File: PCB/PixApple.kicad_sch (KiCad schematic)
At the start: 21 parts, among them J3 Conn_01x17, J4 Conn_01x17, J5 Conn_01x05_Pin, J6 Conn_01x02_Pin, SW1 SW_Push, U1 RP2040

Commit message: CAN bus done?
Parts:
- added J7: Conn_01x01_Pin, symbol Connector:Conn_01x01_Pin
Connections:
- net can/CLKOUT: now also J7.1 (Pin_1)
- net can/CANL: now reaches J6.1 (Pin_1)
- net can/CANH: now reaches J6.2 (Pin_2)
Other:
- sheet can: file can.kicad_sch -> canctrl.kicad_sch
- sheet can ports: added CANH, CANL; removed RXCAN, TXCAN
- note added: "label better"
- moved on the sheet: J6

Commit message: Routing PCB
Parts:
- removed J3, J4: Conn_01x17, symbol Connector_Generic:Conn_01x17
- added D2, D3: LED_Small, LED_SMD:LED_0603_1608Metric_Pad1.05x0.95mm_HandSolder, symbol Device:LED_Small
- added J10, J11, J12, J13, J14, J15, J16, J17, J18, J19, J20, J21, J22, J23, J24, J25, J26, J27: Conn_01x03_Pin, Connector_PinHeader_2.54mm:PinHeader_1x03_P2.54mm_Vertical, symbol Connector:Conn_01x03_Pin
- added J8: Conn_02x03_Odd_Even, Connector_PinHeader_2.54mm:PinHeader_2x03_P2.54mm_Vertical, symbol Connector_Generic:Conn_02x03_Odd_Even
- added J9: Conn_01x04_Pin, Connector_PinHeader_2.54mm:PinHeader_1x04_P2.54mm_Vertical, symbol Connector:Conn_01x04_Pin
- added R13, R14: 220R, Resistor_SMD:R_0603_1608Metric_Pad0.98x0.95mm_HandSolder, symbol Device:R_Small
- C10, C11, C12, C13, C17, C3, C4, C5, C6, C7, C8, C9: footprint (none) -> Capacitor_SMD:C_0603_1608Metric_Pad1.08x0.95mm_HandSolder
- J5: footprint (none) -> Connector_PinHeader_2.54mm:PinHeader_1x05_P2.54mm_Vertical
- J6: footprint (none) -> Connector_PinHeader_2.54mm:PinHeader_1x02_P2.54mm_Vertical
- J7: footprint (none) -> TestPoint:TestPoint_Pad_1.0x1.0mm
- R4, R5, R6: footprint (none) -> Resistor_SMD:R_0603_1608Metric_Pad0.98x0.95mm_HandSolder
- SW1: footprint (none) -> Button_Switch_THT:SW_PUSH_6mm_H5mm
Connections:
- net +3V3: now also D3.2 (A), J10.2 (Pin_2), J11.2 (Pin_2), J12.2 (Pin_2), J13.2 (Pin_2), J14.2 (Pin_2), J15.2 (Pin_2), J16.2 (Pin_2), J17.2 (Pin_2), J18.2 (Pin_2), J19.2 (Pin_2), J20.2 (Pin_2), J21.2 (Pin_2), J22.2 (Pin_2), J23.2 (Pin_2), J24.2 (Pin_2), J25.2 (Pin_2), J26.2 (Pin_2), J27.2 (Pin_2), J8.1 (Pin_1), J9.3 (Pin_3)
- net GND: now also J10.1 (Pin_1), J11.1 (Pin_1), J12.1 (Pin_1), J13.1 (Pin_1), J14.1 (Pin_1), J15.1 (Pin_1), J16.1 (Pin_1), J17.1 (Pin_1), J18.1 (Pin_1), J19.1 (Pin_1), J20.1 (Pin_1), J21.1 (Pin_1), J22.1 (Pin_1), J23.1 (Pin_1), J24.1 (Pin_1), J25.1 (Pin_1), J26.1 (Pin_1), J27.1 (Pin_1), J8.6 (Pin_6), J9.4 (Pin_4), R13.1, R14.2
- net GPIO0: now also J18.3 (Pin_3)
- net GPIO1: now also J19.3 (Pin_3)
- net GPIO12: now also J26.3 (Pin_3)
- net GPIO13: now also J27.3 (Pin_3)
- net GPIO2: now also J20.3 (Pin_3)
- net GPIO3: now also J21.3 (Pin_3)
- net GPIO4: now also J22.3 (Pin_3)
- net GPIO5: now also J23.3 (Pin_3)
- net GPIO6: now also J24.3 (Pin_3)
- net GPIO7: now also J25.3 (Pin_3)
- net GIPO26 renamed ADC0
- net ADC0: now also J14.3 (Pin_3)
- net GPIO10 renamed SPI1_SCK
- net SPI1_SCK: now also J8.3 (Pin_3)
- net GPIO11 renamed SPI1_TX
- net SPI1_TX: now also J8.5 (Pin_5)
- net GPIO14 renamed I2C1_SDA
- net I2C1_SDA: now also J9.1 (Pin_1)
- net GPIO15 renamed I2C1_SCL
- net I2C1_SCL: now also J9.2 (Pin_2)
- net GPIO16: no longer names the net of U1.27 (GPIO16)
- net GPIO16: now also D2.2 (A)
- net GPIO17 renamed CAN_INT
- net GPIO18 renamed SPI0_SCK
- net GPIO19 renamed SPI0_TX
- net GPIO20 renamed SPI0_RX
- net GPIO21 renamed SPI0_CSn
- net GPIO22 renamed PWM0
- net PWM0: now also J10.3 (Pin_3)
- net GPIO23 renamed PWM1
- net PWM1: now also J11.3 (Pin_3)
- net GPIO24 renamed PWM2
- net PWM2: now also J12.3 (Pin_3)
- net GPIO25 renamed PWM3
- net PWM3: now also J13.3 (Pin_3)
- net GPIO27 renamed ADC1
- net ADC1: now also J15.3 (Pin_3)
- net GPIO28 renamed ADC2
- net ADC2: now also J16.3 (Pin_3)
- net GPIO29 renamed ADC3
- net ADC3: now also J17.3 (Pin_3)
- net GPIO8 renamed SPI1_RX
- net SPI1_RX: now also J8.2 (Pin_2)
- net GPIO9 renamed SPI1_CSn
- net SPI1_CSn: now also J8.4 (Pin_4)
- new net: D3.1 (K), R14.1
- new net: D2.1 (K), R13.2
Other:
- moved on the sheet: C10, C11, C12, C13, C17, C3, C4, C5, C6, C7, C8, C9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

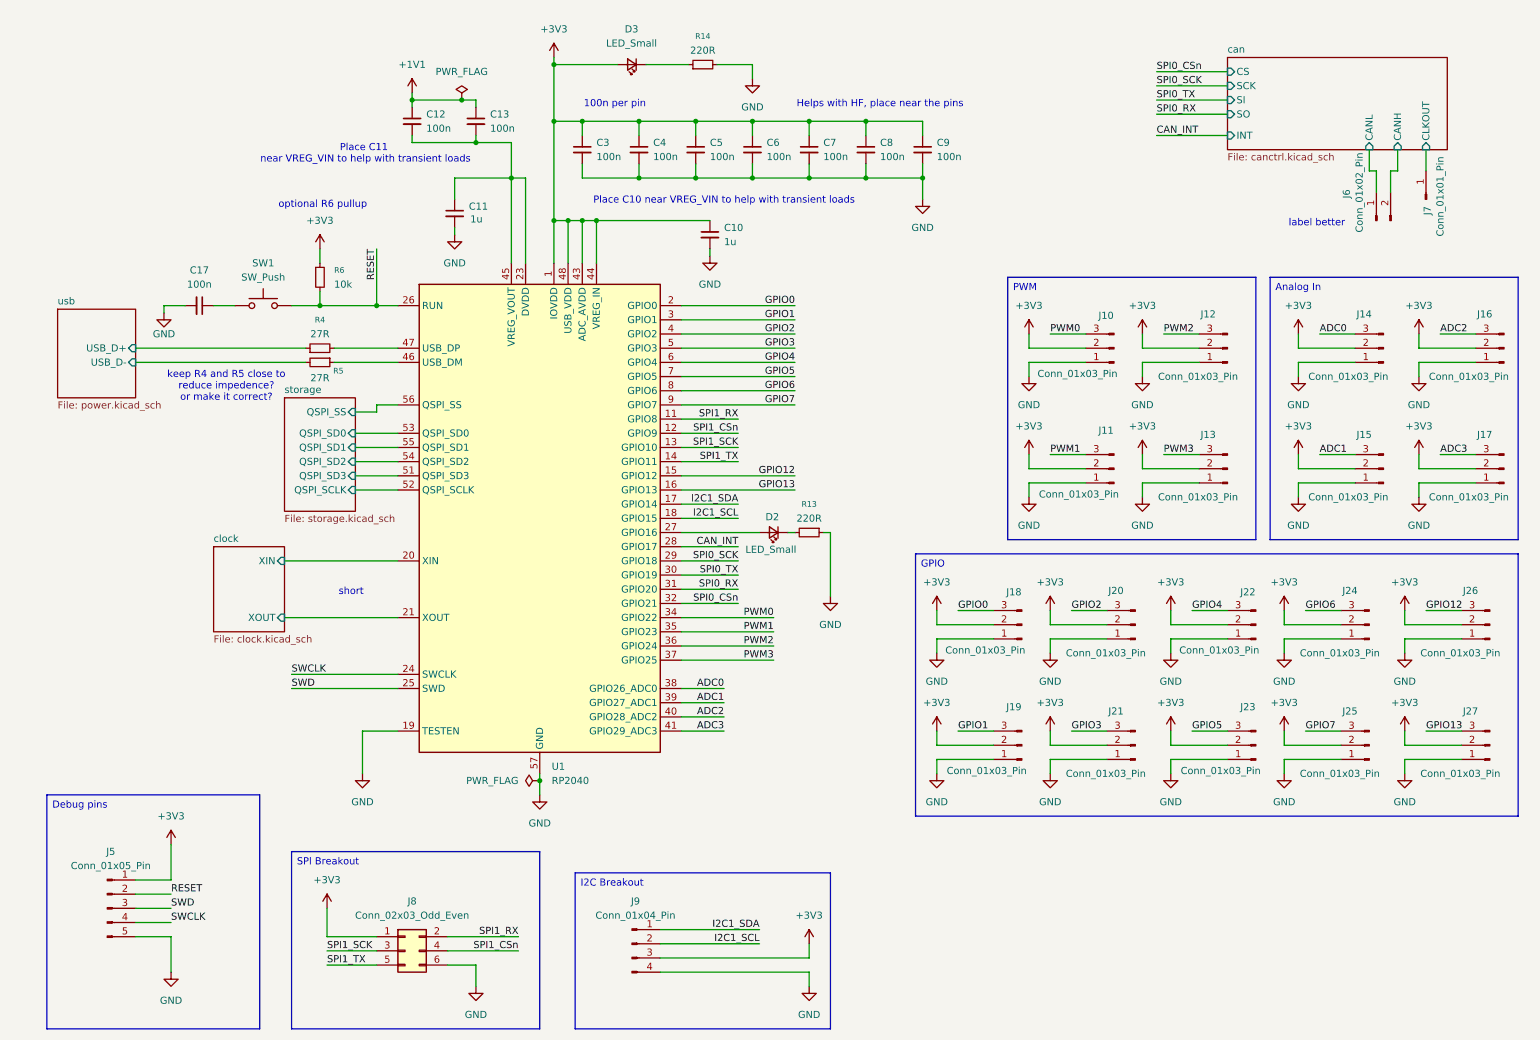
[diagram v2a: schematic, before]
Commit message: PCB routing, better placement
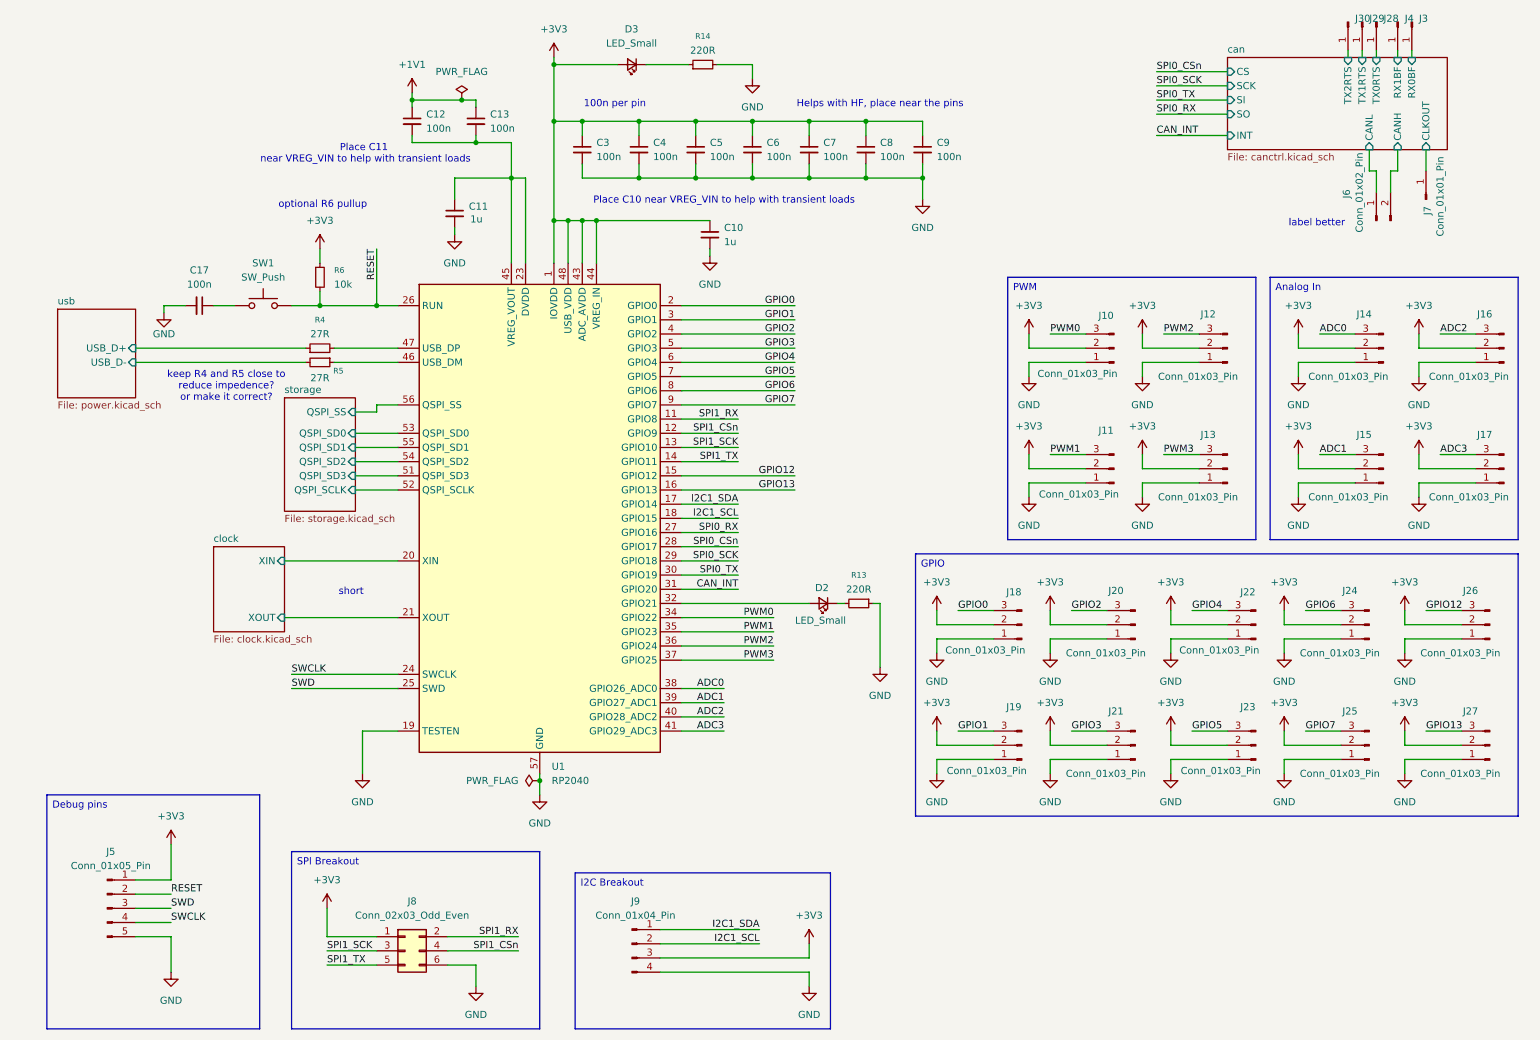
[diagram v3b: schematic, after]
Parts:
- added J28, J29, J3, J30, J4: Conn_01x01_Pin, TestPoint:TestPoint_Pad_1.0x1.0mm, symbol Connector:Conn_01x01_Pin
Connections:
- net CAN_INT: now also U1.31 (GPIO20); no longer U1.28 (GPIO17)
- net SPI0_CSn: now also U1.28 (GPIO17); no longer U1.32 (GPIO21)
- net SPI0_RX: now also U1.27 (GPIO16); no longer U1.31 (GPIO20)
- net at D2.2 (A): now also U1.32 (GPIO21); no longer U1.27 (GPIO16)
- new net can/RX0BF: J3.1 (Pin_1)
- new net can/RX1BF: J4.1 (Pin_1)
- new net can/TX0RTS: J28.1 (Pin_1)
- new net can/TX1RTS: J29.1 (Pin_1)
- new net can/TX2RTS: J30.1 (Pin_1)
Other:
- sheet can ports: added RX0BF, RX1BF, TX0RTS, TX1RTS, TX2RTS; removed none
- moved on the sheet: D2, R13

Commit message: Finished PCB routing
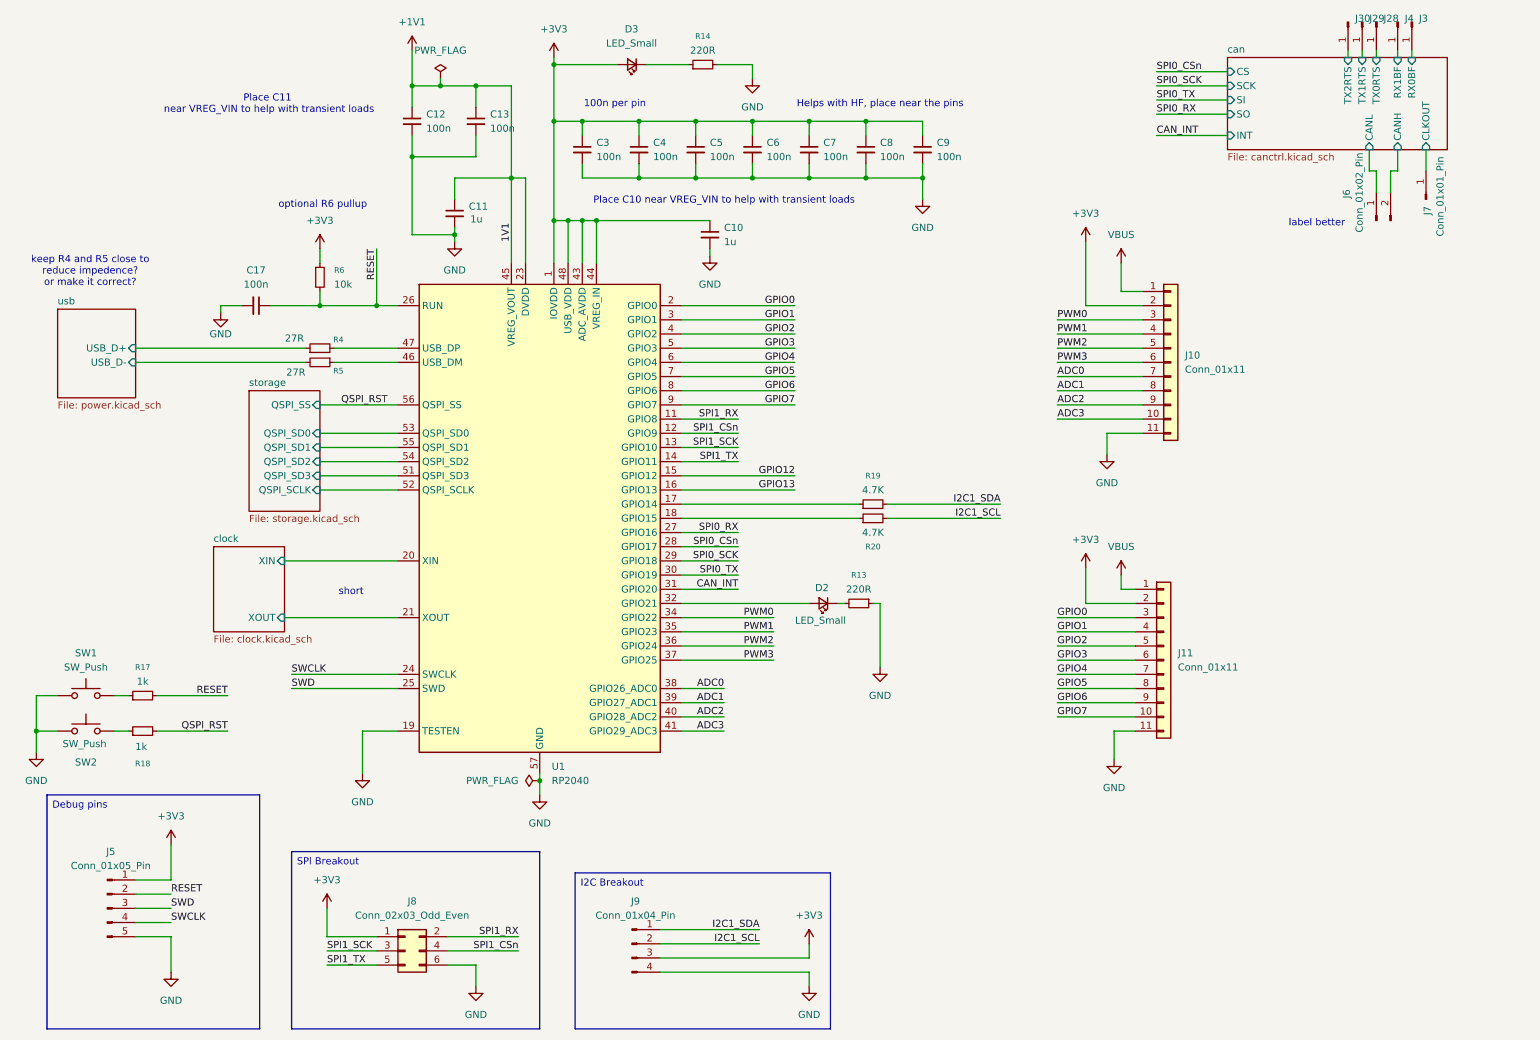
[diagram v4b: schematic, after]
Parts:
- removed J10, J11, J12, J13, J14, J15, J16, J17, J18, J19, J20, J21, J22, J23, J24, J25, J26, J27: Conn_01x03_Pin, Connector_PinHeader_2.54mm:PinHeader_1x03_P2.54mm_Vertical, symbol Connector:Conn_01x03_Pin
- added J10, J11: Conn_01x11, Connector_PinHeader_2.54mm:PinHeader_1x11_P2.54mm_Vertical, symbol Connector_Generic:Conn_01x11
- added R17, R18: 1k, Resistor_SMD:R_0603_1608Metric_Pad0.98x0.95mm_HandSolder, symbol Device:R_Small
- added R19, R20: 4.7K, Resistor_SMD:R_0603_1608Metric_Pad0.98x0.95mm_HandSolder, symbol Device:R_Small
- added SW2: SW_Push, Button_Switch_THT:SW_PUSH_6mm, symbol Switch:SW_Push
- SW1: footprint Button_Switch_THT:SW_PUSH_6mm_H5mm -> Button_Switch_THT:SW_PUSH_6mm
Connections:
- net +1V1: now also C11.1, U1.23 (DVDD), U1.45 (VREG_VOUT), U1.50 (DVDD)
- net +3V3: now also J10.2 (Pin_2), J11.2 (Pin_2)
- net ADC0: now also J10.7 (Pin_7)
- net ADC1: now also J10.8 (Pin_8)
- net ADC2: now also J10.9 (Pin_9)
- net ADC3: now also J10.10 (Pin_10)
- net GND: now also C12.2, C13.2, SW1.1, J10.11 (Pin_11), J11.11 (Pin_11), SW2.1
- net GPIO0: now also J11.3 (Pin_3)
- net GPIO1: now also J11.4 (Pin_4)
- net GPIO2: now also J11.5 (Pin_5)
- net GPIO3: now also J11.6 (Pin_6)
- net GPIO4: now also J11.7 (Pin_7)
- net GPIO5: now also J11.8 (Pin_8)
- net GPIO6: now also J11.9 (Pin_9)
- net GPIO7: now also J11.10 (Pin_10)
- net I2C1_SCL: now also R20.2; no longer U1.18 (GPIO15)
- net I2C1_SDA: now also R19.2; no longer U1.17 (GPIO14)
- net PWM0: now also J10.3 (Pin_3)
- net PWM1: now also J10.4 (Pin_4)
- net PWM2: now also J10.5 (Pin_5)
- net PWM3: now also J10.6 (Pin_6)
- net RESET: now also C17.1, R17.2; no longer SW1.2
- net storage/QSPI_SS renamed QSPI_RST
- net QSPI_RST: now also R18.2
- new net: R20.1, U1.18 (GPIO15)
- new net: R19.1, U1.17 (GPIO14)
- new net: R18.1, SW2.2
- new net: R17.1, SW1.2
- new net VBUS: J10.1 (Pin_1), J11.1 (Pin_1)
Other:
- moved on the sheet: C17
